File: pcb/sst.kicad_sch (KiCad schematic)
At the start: 36 parts, among them X1 CONN_INPUTS, X2 CONN_PWR, X3 CONN_SPI, X4 CONN_I2C, X5 CONN_INPUTS

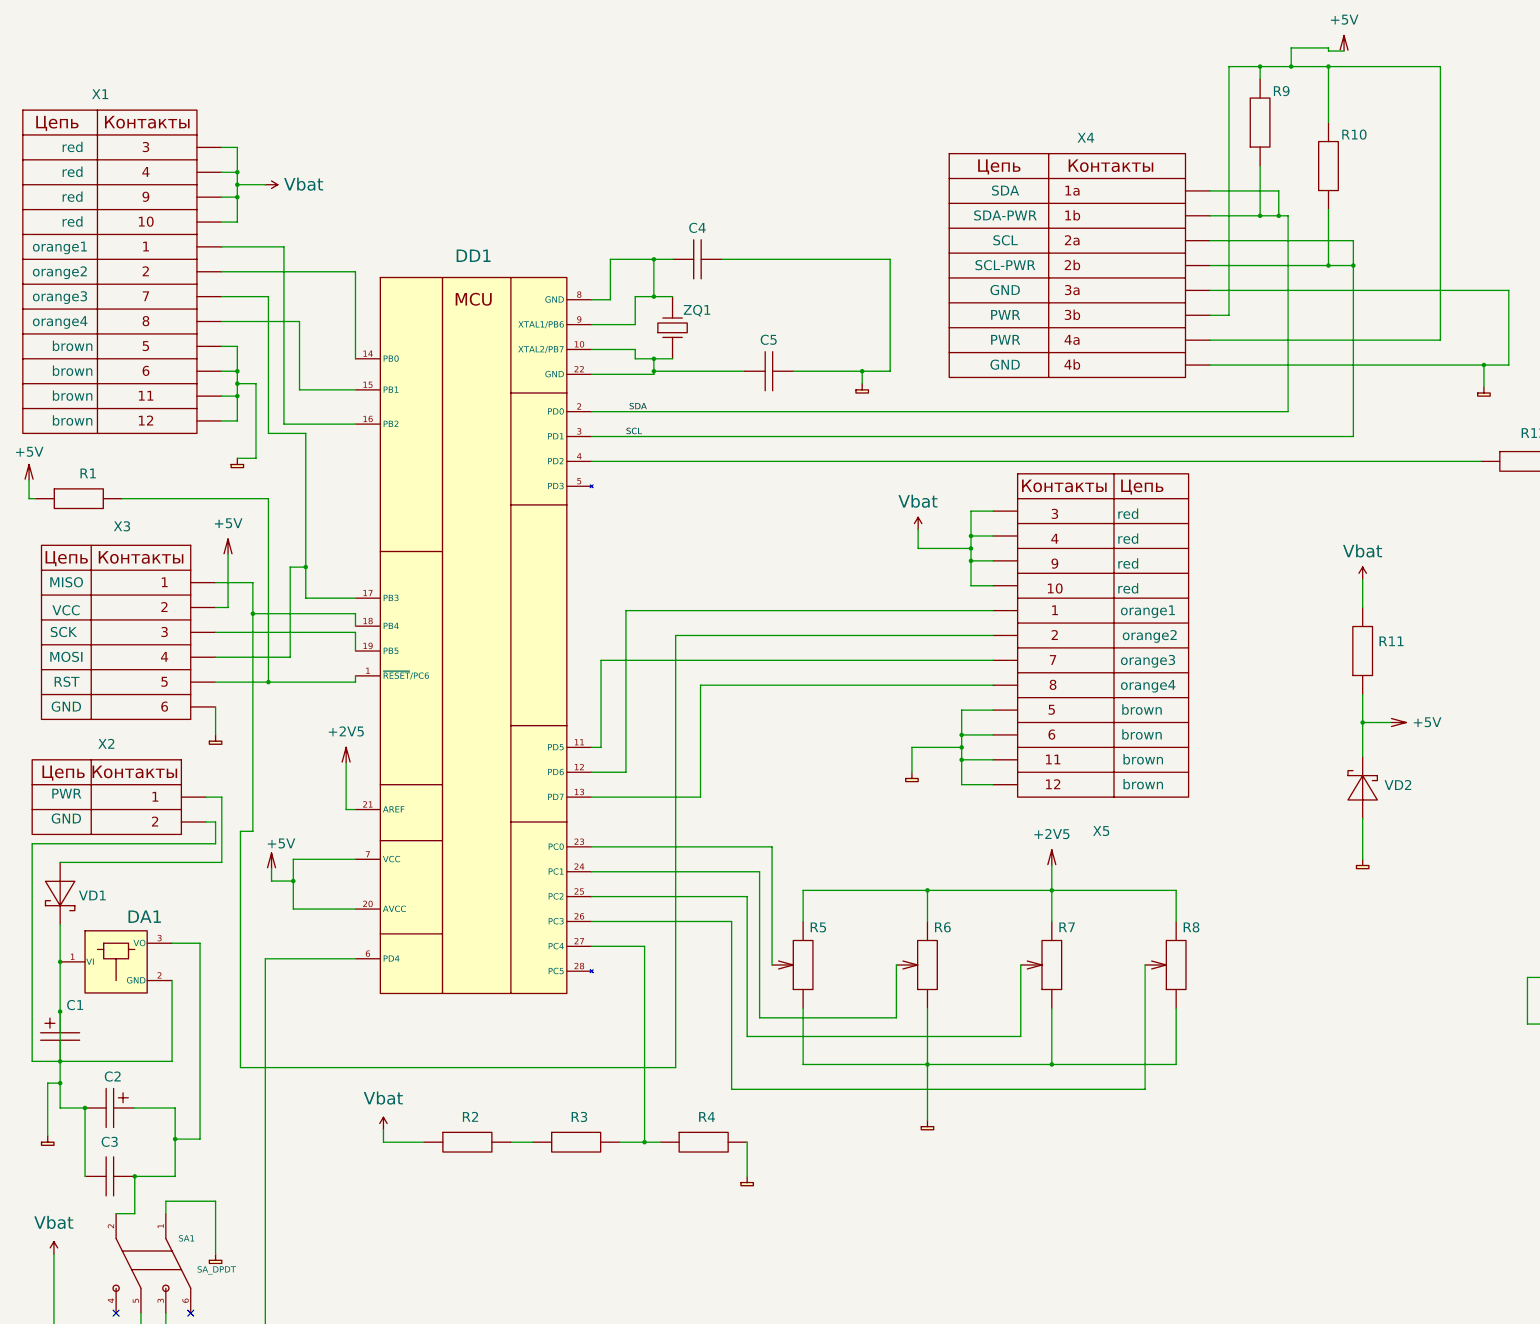
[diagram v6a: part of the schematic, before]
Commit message: Попроавки в Э3, другой символ батареи
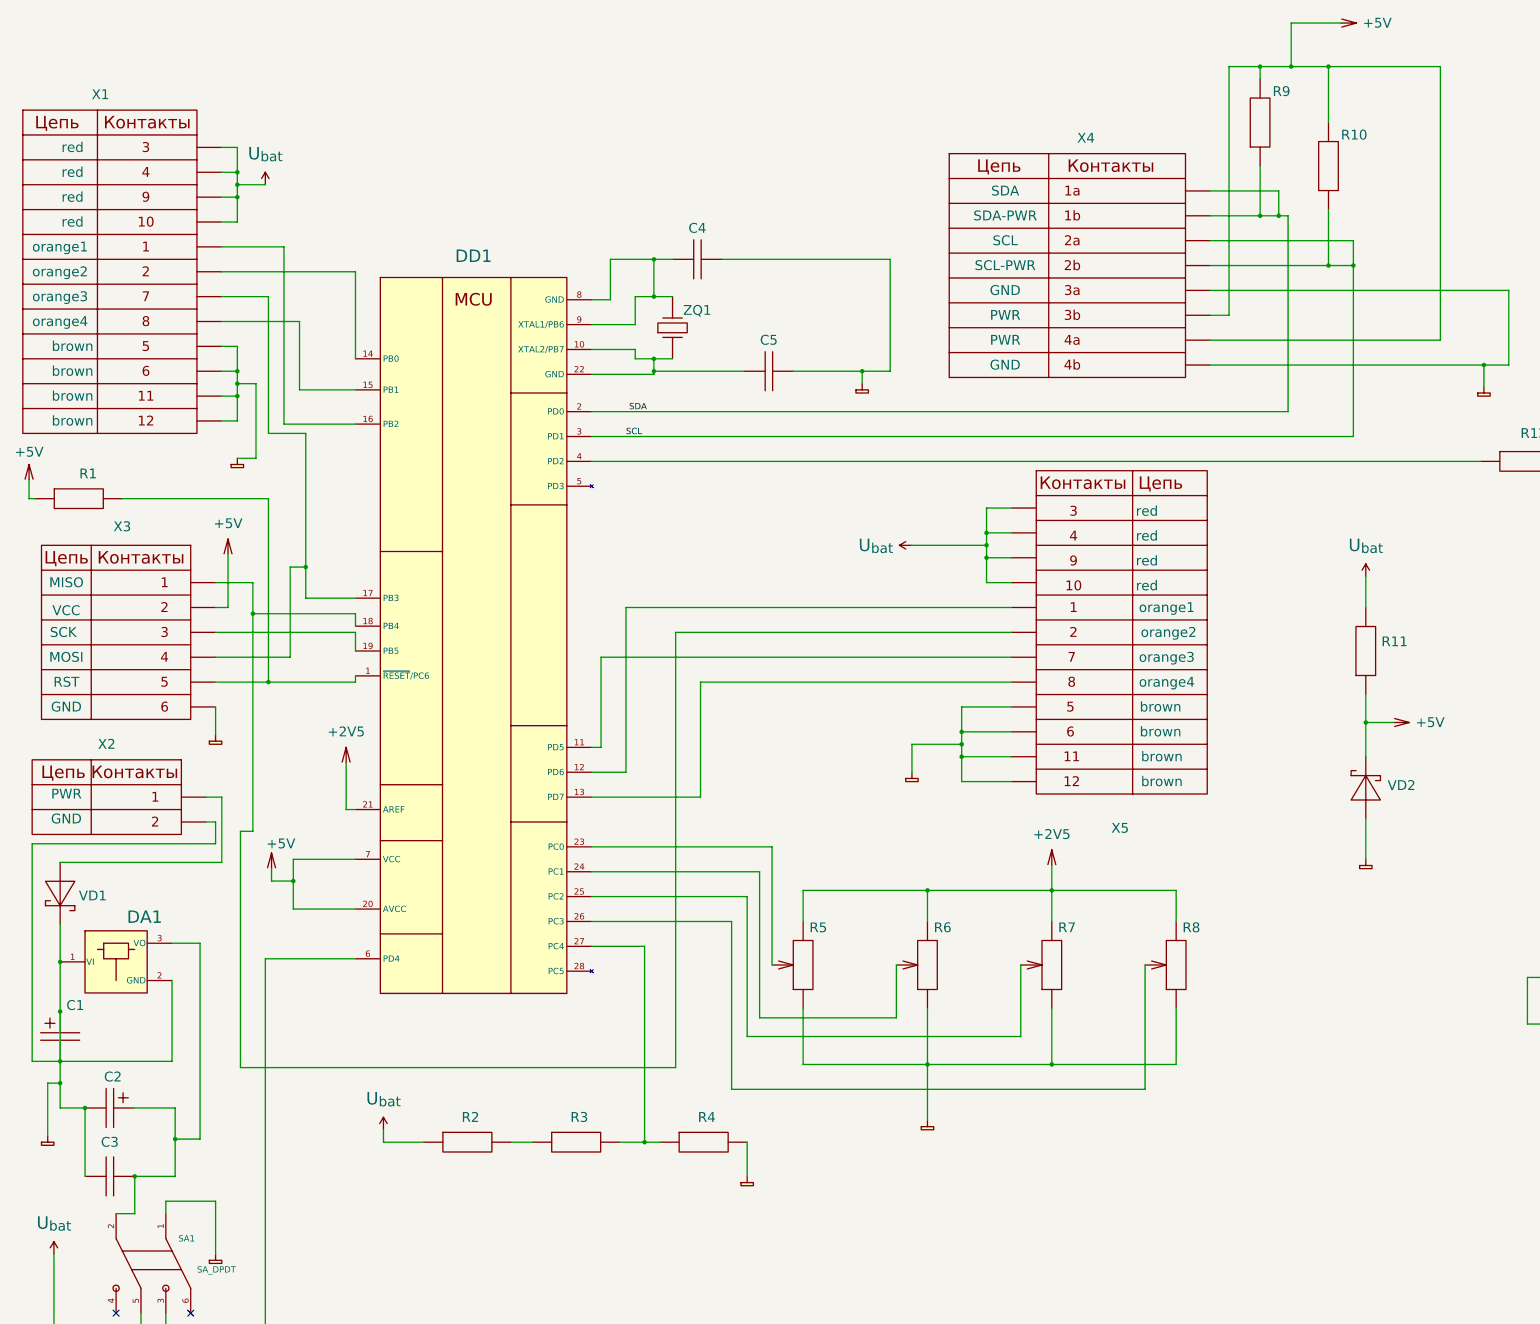
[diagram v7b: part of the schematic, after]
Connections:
- net Vbat renamed U_{bat}
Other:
- moved on the sheet: R11, VD2, X5

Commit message: [2024-12-24 15:48] coursework for this day
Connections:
- net GND: no longer C1.1, DA1.1 (VI), VD1.1 (K)
- new net: C1.1, DA1.1 (VI), VD1.1 (K)
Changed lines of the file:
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@@
-	)
-	(junction
-		(at 31.75 214.63)
-		(diameter 0)
-		(color 0 0 0 0)
 	)
 	(junction
@@
 		)
 		(stroke
-			(width 0)
-			(type default)
-		)
-	)
-	(wire
-		(pts
-			(xy 31.75 224.79) (xy 31.75 214.63)
-		)
-		(stroke
